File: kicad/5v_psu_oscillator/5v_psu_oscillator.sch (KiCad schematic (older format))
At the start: 30 parts, among them P1 CONN_01X03, SW1 DPST, T1 BV 030-7329.0 T, U1 LT1017, U2 74HC08, U3 LM2675N-5.0, U4 74HC4024

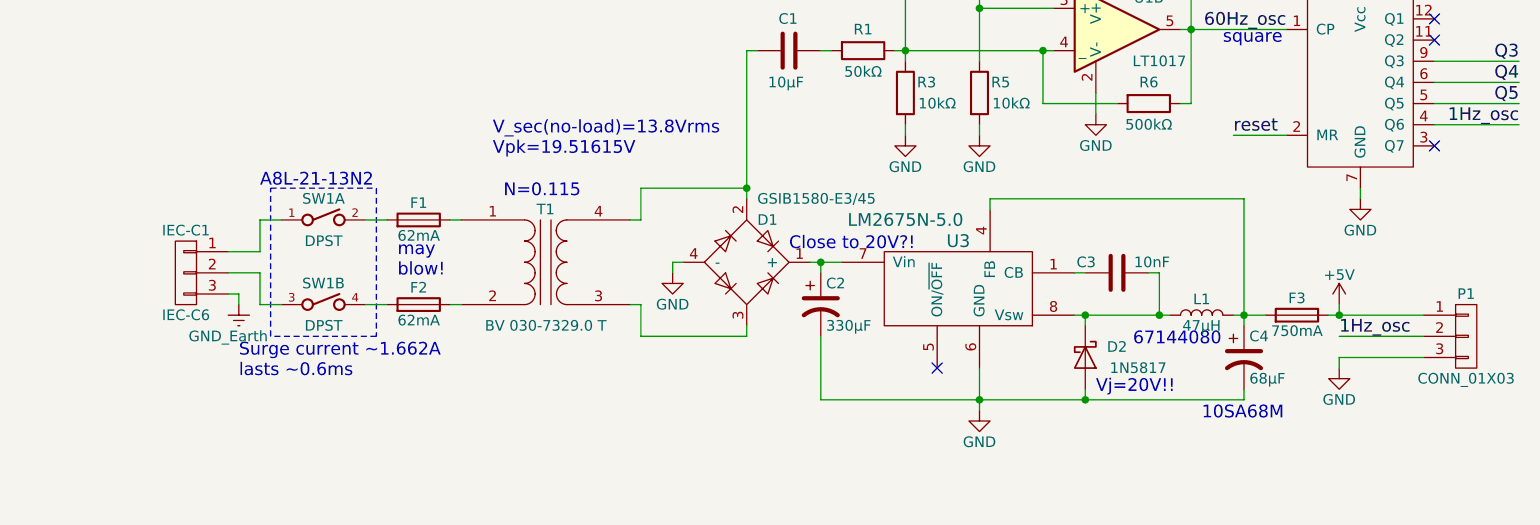
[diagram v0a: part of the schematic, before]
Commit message: Associate more footprints
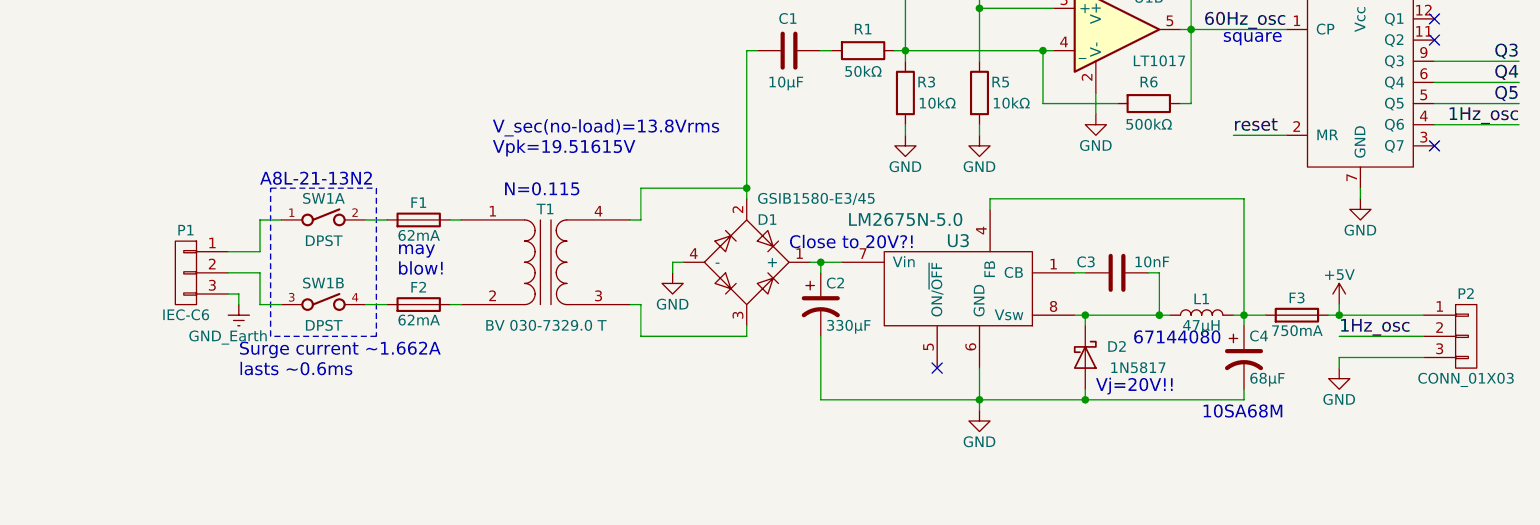
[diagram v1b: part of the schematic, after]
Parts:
- P2: renamed from P1; footprint (none) -> Pin_Headers:Pin_Header_Angled_1x03_Pitch2.54mm
- U1: footprint (none) -> Housings_DIP:DIP-8_W7.62mm_LongPads
- U2, U4: footprint (none) -> Housings_DIP:DIP-14_W7.62mm_LongPads
- renumbered IEC-C1 to P1
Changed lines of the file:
@@
 $EndComp
 $Comp
-L CONN_01X03 IEC-C1
+L CONN_01X03 P1
 U 1 1 5906AD4D
 P 2500 3950
-F 0 "IEC-C1" H 2500 4150 50  0000 C CNN
+F 0 "P1" H 2500 4150 50  0000 C CNN
 F 1 "IEC-C6" H 2500 3750 50  0000 C CNN
 F 2 "" H 2500 3950 50  0001 C CNN
@@
 $EndComp
 $Comp
-L CONN_01X03 P1
+L CONN_01X03 P2
 U 1 1 5906B6FF
 P 8550 4250
-F 0 "P1" H 8550 4450 50  0000 C CNN
+F 0 "P2" H 8550 4450 50  0000 C CNN
 F 1 "CONN_01X03" H 8550 4050 50  0000 C CNN
-F 2 "" H 8550 4250 50  0001 C CNN
+F 2 "Pin_Headers:Pin_Header_Angled_1x03_Pitch2.54mm" H 8550 4250 50  0001 C CNN
 F 3 "" H 8550 4250 50  0000 C CNN
 	1    8550 4250
@@
 F 0 "U1" H 7050 2950 50  0000 C CNN
 F 1 "LT1017" H 7100 2650 50  0000 C CNN
-F 2 "" H 6900 2800 50  0001 C CNN
+F 2 "Housings_DIP:DIP-8_W7.62mm_LongPads" H 6900 2800 50  0001 C CNN
 F 3 "" H 6900 2800 50  0000 C CNN
 	2    6900 2800
@@
 F 0 "U2" H 6100 1150 50  0000 C CNN
 F 1 "74HC08" H 6100 1050 50  0000 C CNN
-F 2 "" H 6100 1100 50  0001 C CNN
+F 2 "Housings_DIP:DIP-14_W7.62mm_LongPads" H 6100 1100 50  0001 C CNN
 F 3 "" H 6100 1100 50  0000 C CNN
 	2    6100 1100
@@
 F 0 "U2" H 6100 1600 50  0000 C CNN
 F 1 "74HC08" H 6100 1500 50  0000 C CNN
-F 2 "" H 6100 1550 50  0001 C CNN
+F 2 "Housings_DIP:DIP-14_W7.62mm_LongPads" H 6100 1550 50  0001 C CNN
 F 3 "" H 6100 1550 50  0000 C CNN
 	3    6100 1550
@@
 F 0 "U2" H 7400 1350 50  0000 C CNN
 F 1 "74HC08" H 7400 1250 50  0000 C CNN
-F 2 "" H 7400 1300 50  0001 C CNN
+F 2 "Housings_DIP:DIP-14_W7.62mm_LongPads" H 7400 1300 50  0001 C CNN
 F 3 "" H 7400 1300 50  0000 C CNN
 	4    7400 1300
@@
 F 0 "U2" H 2050 7450 50  0000 C CNN
 F 1 "74HC08" H 2050 7350 50  0000 C CNN
-F 2 "" H 2050 7400 50  0001 C CNN
+F 2 "Housings_DIP:DIP-14_W7.62mm_LongPads" H 2050 7400 50  0001 C CNN
 F 3 "" H 2050 7400 50  0000 C CNN
 	1    2050 7400
@@
 F 0 "U4" H 8150 3600 60  0000 C CNN
 F 1 "74HC4024" H 8300 3500 60  0000 C CNN
-F 2 "" H 8050 3000 60  0001 C CNN
+F 2 "Housings_DIP:DIP-14_W7.62mm_LongPads" H 8050 3000 60  0001 C CNN
 F 3 "" H 8050 3000 60  0001 C CNN
 	1    8050 3050
@@
 F 0 "U1" H 1050 7300 50  0000 C CNN
 F 1 "LT1017" H 1100 7000 50  0000 C CNN
-F 2 "" H 900 7150 50  0001 C CNN
+F 2 "Housings_DIP:DIP-8_W7.62mm_LongPads" H 900 7150 50  0001 C CNN
 F 3 "" H 900 7150 50  0000 C CNN
 	1    900  7150

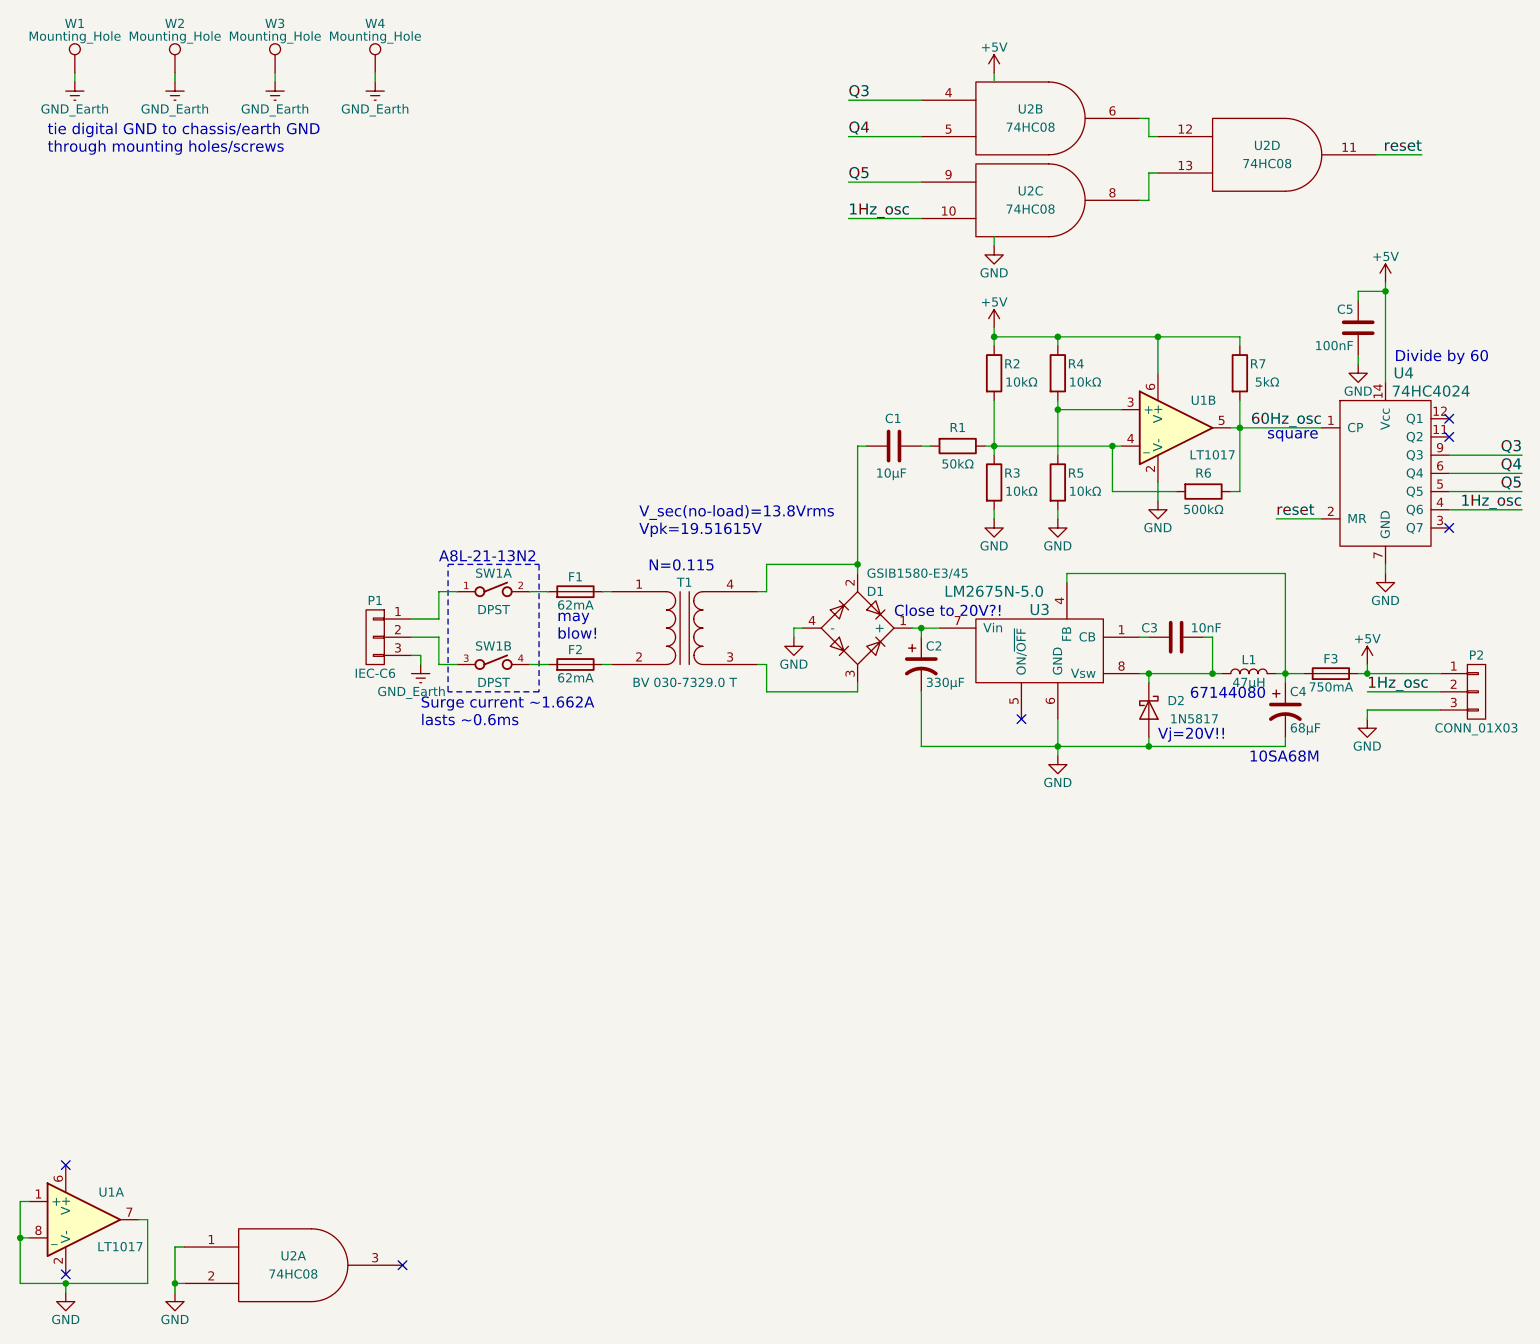
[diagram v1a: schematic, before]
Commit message: Associate some more footprints
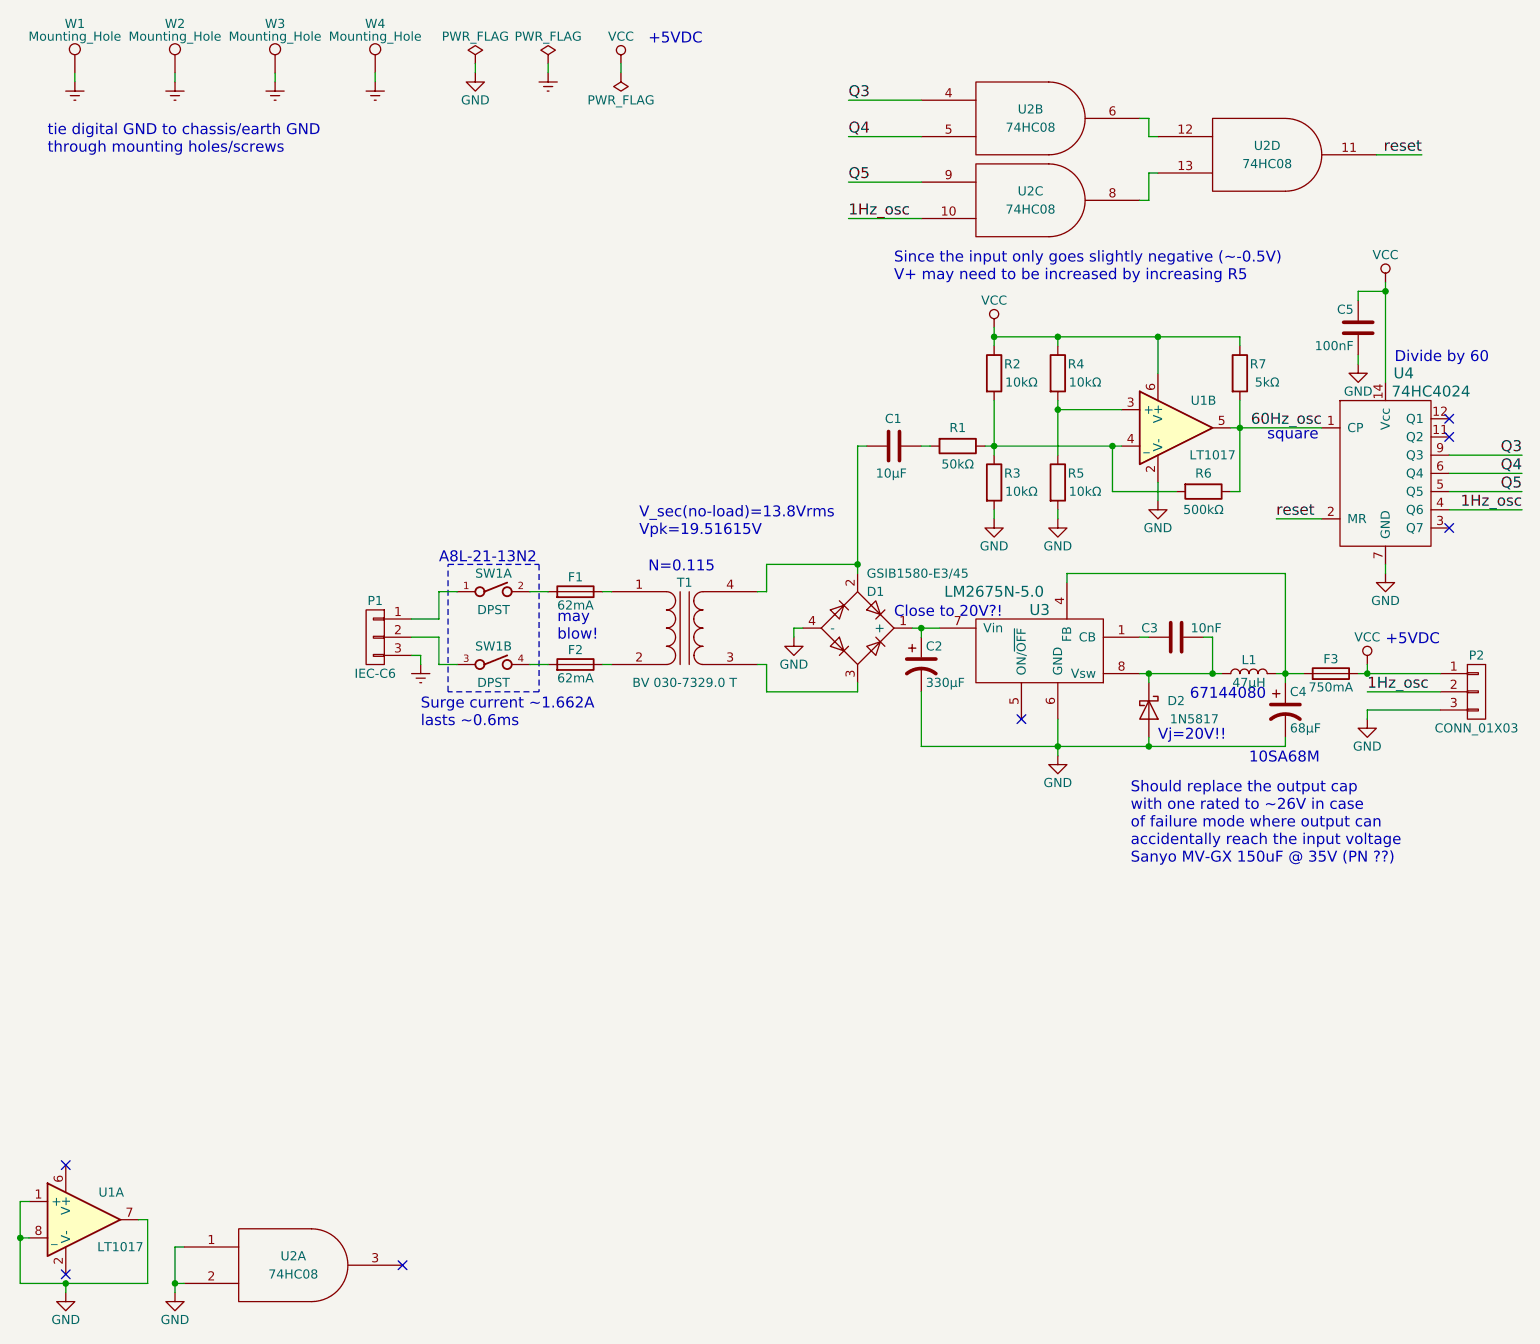
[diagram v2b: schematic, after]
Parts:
- C1: footprint (none) -> Capacitors_THT:C_Disc_D5.0mm_W2.5mm_P2.50mm
- C2: footprint (none) -> Capacitors_THT:CP_Radial_D10.0mm_P5.00mm
- C3: footprint (none) -> Capacitors_THT:C_Disc_D3.4mm_W2.1mm_P2.50mm
- C4: footprint (none) -> Capacitors_THT:CP_Radial_D6.3mm_P2.50mm
- C5: footprint (none) -> Capacitors_THT:C_Disc_D3.8mm_W2.6mm_P2.50mm
- D2: footprint (none) -> Diodes_THT:D_DO-41_SOD81_P10.16mm_Horizontal
- F1, F2, F3: footprint (none) -> Resistors_THT:R_Axial_DIN0309_L9.0mm_D3.2mm_P12.70mm_Horizontal
- R1, R2, R3, R4, R5, R6, R7: footprint (none) -> Resistors_THT:R_Axial_DIN0207_L6.3mm_D2.5mm_P7.62mm_Horizontal
- W1, W2, W3, W4: footprint (none) -> Mounting_Holes:MountingHole_3.2mm_M3_Pad
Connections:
- net Earth: now reaches P1.3 (P3)
- net Earth: now also W1.1, W2.1, W3.1, W4.1
- net +5V renamed VCC
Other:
- note added: "+5VDC"
- note added: "Should replace the output cap\nwith one rated to ~~26V in case\nof failure mode where output can\naccidentally reach the input voltage\nSanyo MV-GX 150uF @ 35V (PN ??)"
- note added: "Since the input only goes slightly negative (~~-0.5V)\nV+ may need to be increased by increasing R5"
